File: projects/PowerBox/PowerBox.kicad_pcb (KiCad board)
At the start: 2 copper layers, 91.4 x 56.9 mm, 119 parts, among them CON1 USB-MICRO, CON2 USB-A-Jack, CON3 USB-MINI-B-Vert, IC1 LM358, IC2 LM358, IC3 LM358, P1 CONN_2, P11 CONN_10, P12 CONN_8, P13 CONN_8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

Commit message: pcb layout still in progress
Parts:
- moved D14 45.5 mm to (178.3, 110.5), turned to 180 degrees
- moved R32 45.5 mm to (178.3, 110.5), turned to 180 degrees
- moved D13 45.3 mm to (178.3, 106.7), turned to 180 degrees
- moved R31 45.3 mm to (178.3, 106.7), turned to 180 degrees
- moved JP2 23.6 mm to (155.2, 114.6)
- moved R20 18.4 mm to (117.9, 88.6)
- moved R16 16.9 mm to (119.4, 84.1), turned to 270 degrees
- moved R17 15.8 mm to (132.8, 81.0)
- moved R19 15.8 mm to (120.4, 93.2)
- moved R21 14.2 mm to (122.9, 83.1)
- moved R23 13.9 mm to (122.9, 88.6)
- moved R18 10.7 mm to (125.5, 93.2)
- moved R25 8.64 mm to (141.7, 114.6)
- moved R22 8.44 mm to (128.0, 88.6)
- moved R28 7.77 mm to (145.8, 106.7)
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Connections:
- net D7 renamed Clock
- U1 pad 10: V_MP -> VREG_in
- U3 pad 10: V_MP -> VREG_in
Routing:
- net VREG_in: track 111.4 -> 283.0 mm, vias 6 -> 9
- net Net-(JP1-Pad2): track 0.00 -> 56.1 mm, vias 0 -> 2
- net DIG1: track 0.00 -> 41.9 mm, vias 0 -> 1
- net SEGA: track 0.00 -> 41.8 mm
- net Net-(C4-Pad1): track 27.2 -> 63.3 mm, vias 0 -> 1
- net Net-(R7-Pad1): track 0.00 -> 35.9 mm
- net SEGE: track 0.00 -> 34.2 mm, vias 0 -> 2
- net SEGF: track 0.00 -> 32.7 mm, vias 0 -> 2
- net SEGB: track 0.00 -> 32.6 mm, vias 0 -> 2
- net SEGC: track 0.27 -> 31.8 mm, vias 0 -> 2
- net SEGD: track 0.00 -> 31.2 mm, vias 0 -> 2
- net TXLED: track 0.00 -> 30.1 mm, vias 0 -> 2
- net Net-(R8-Pad1): track 0.00 -> 27.9 mm
- net SEGDP: track 0.00 -> 24.4 mm
- net DIG2: track 0.00 -> 23.5 mm
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
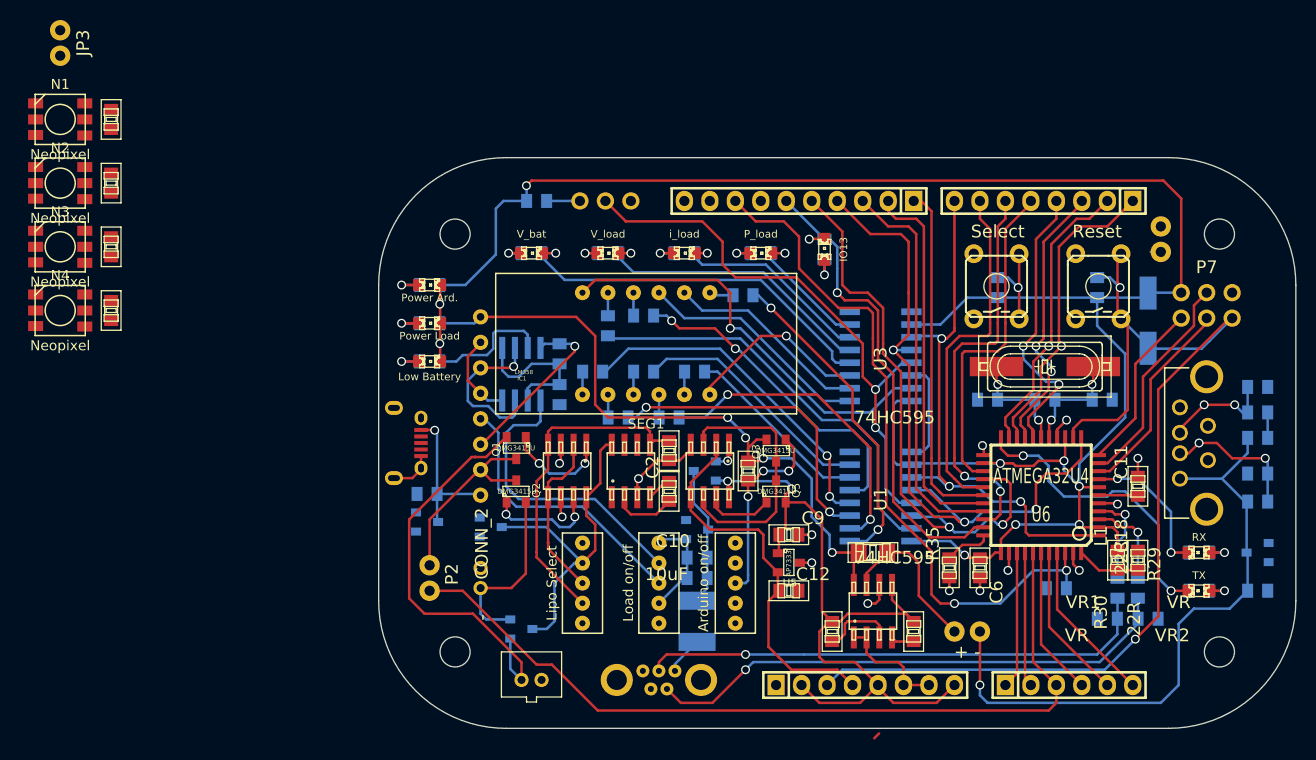
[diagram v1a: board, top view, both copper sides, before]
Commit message: pcb layout most traces done
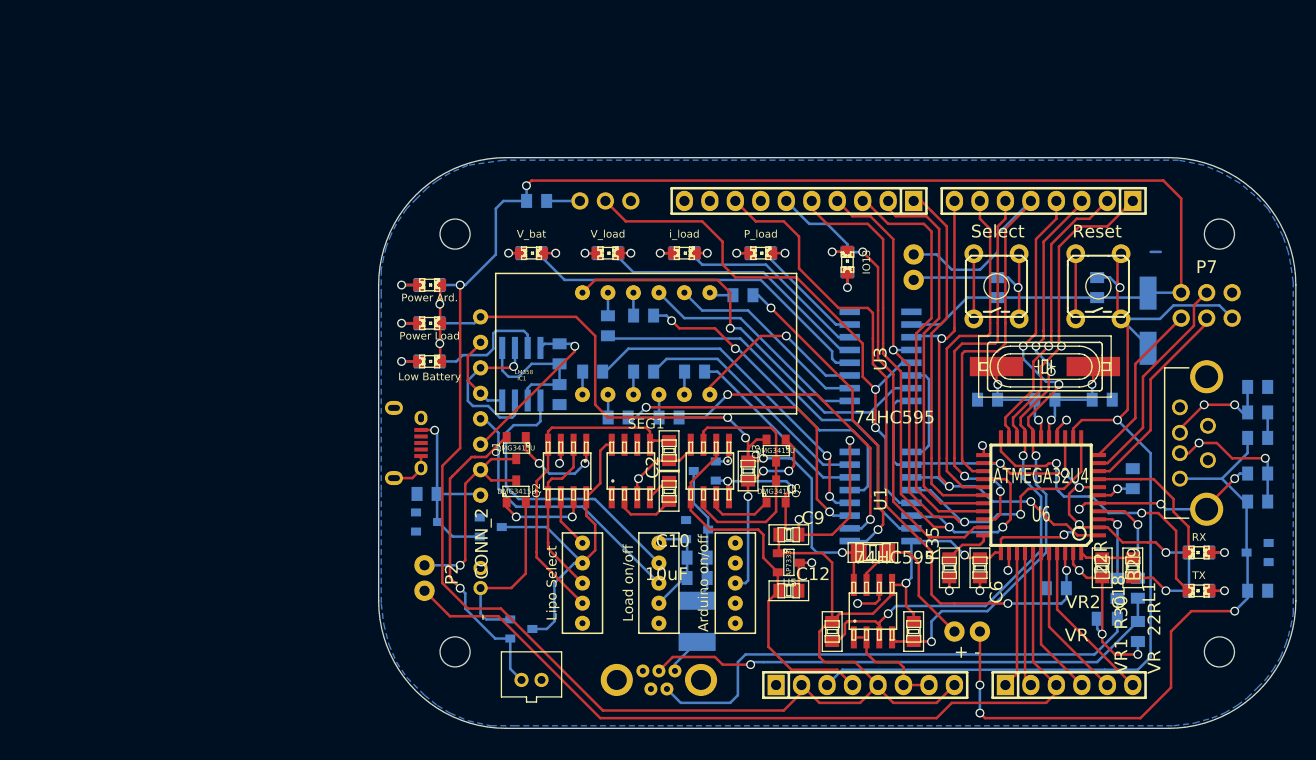
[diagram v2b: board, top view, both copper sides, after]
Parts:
- removed C13, C14, C15, C17: 100nF, frep:C0805
- removed JP3: JUMPER, frep:Pin_Proto_Straight_1x02
- removed N1, N2, N3, N4: Neopixel, frep:Neopixel
- C11: moved to B.Cu
- moved JP5 24.8 mm to (149.9, 78.2)
- moved VR2 4.06 mm to (169.2, 113.3), turned to 180 degrees
- moved C18 3.64 mm to (168.7, 108.2), turned to 270 degrees
- moved VR1 3.30 mm to (172.2, 114.6), turned to 270 degrees
- moved D16 2.62 mm to (143.3, 77.7)
- moved R34 2.62 mm to (143.3, 77.7)
- moved R29 2.03 mm to (170.2, 110.2)
- moved R30 2.03 mm to (172.2, 110.2)
- moved L1 1.70 mm to (171.7, 108.2), turned to 270 degrees
- moved C11 0.92 mm to (171.7, 99.3)
- moved JP4 0.51 mm to (101.1, 109.2)
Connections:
- net Clock renamed D7
- net IO_12 renamed Data
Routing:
- net VREG_in: track 283.0 -> 352.5 mm, vias 9 -> 13
- net GND: track 80.7 -> 147.2 mm, vias 21 -> 24
- net D2/SDA: track 35.4 -> 68.0 mm, vias 2 -> 4
- net D3/SCL: track 30.8 -> 60.9 mm, vias 2 -> 4
- net D4: track 33.3 -> 49.5 mm
- net Net-(D4-Pad1): track 41.3 -> 31.4 mm, vias 0 -> 1
- net Net-(JP5-Pad2): track 10.0 -> 17.8 mm
- net RESET: track 109.3 -> 101.7 mm
- net Net-(C1-Pad1): track 15.2 -> 19.9 mm
- net Net-(C4-Pad1): track 63.3 -> 65.8 mm, vias 1 -> 3
- net IO_10: track 39.8 -> 42.1 mm
- net V_BATT: track 19.7 -> 22.0 mm, vias 0 -> 1
- net Net-(IC2-Pad7): track 11.3 -> 9.43 mm
- net IO_9: track 37.8 -> 39.6 mm
- net Latch: track 68.1 -> 66.4 mm
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- added copper zone on B.Cu, net GND

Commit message: traces done
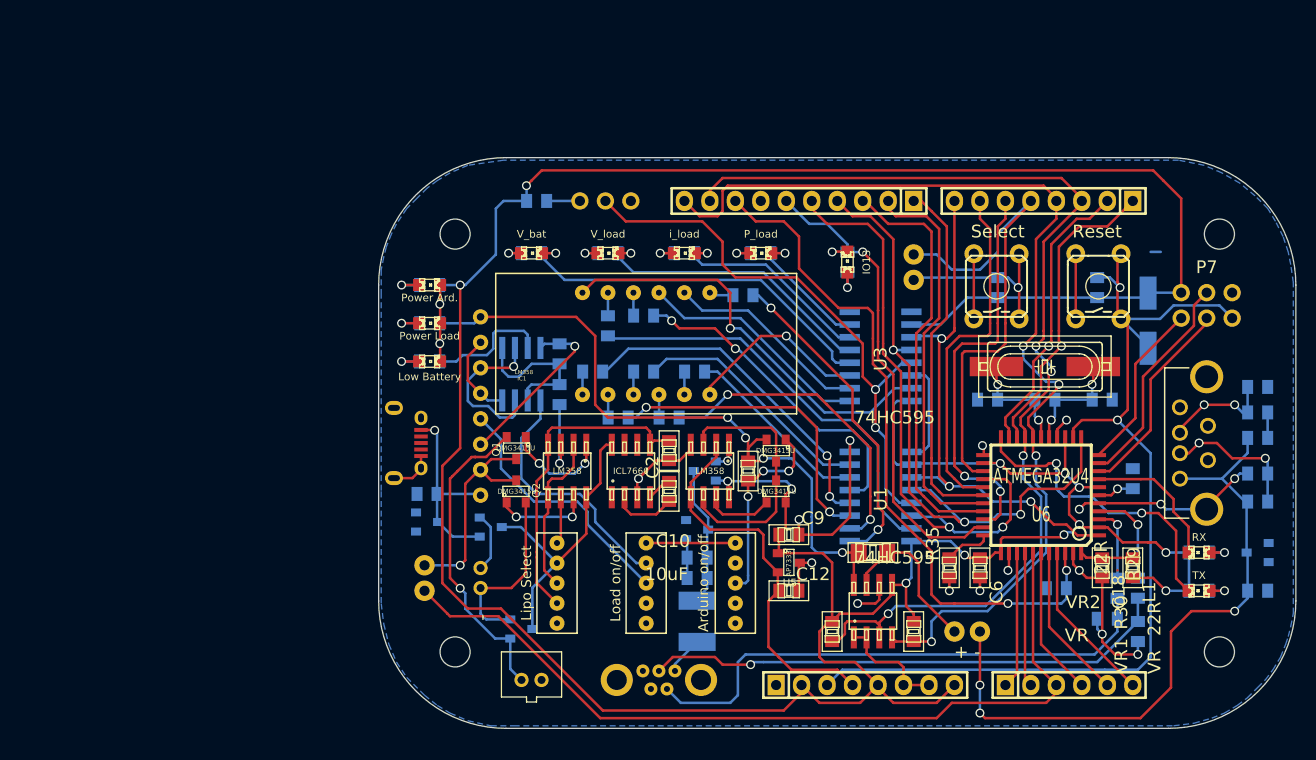
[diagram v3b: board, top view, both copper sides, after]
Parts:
- moved S1 2.54 mm to (114.3, 109.7)
- moved S2 1.27 mm to (123.2, 109.7)
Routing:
- net D3/SCL: track 60.9 -> 101.9 mm
- net D2/SDA: track 68.0 -> 107.7 mm
- net GND: track 147.2 -> 160.8 mm
- net V+: track 33.5 -> 29.0 mm
- net En: track 29.7 -> 25.3 mm
- net Enable: track 28.5 -> 26.3 mm
- net V-: track 34.3 -> 33.3 mm
- net LipoSwitch: track 18.0 -> 17.1 mm
- net VREG_in: track 352.5 -> 353.4 mm

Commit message: pcb still not finished
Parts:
- P7: value CONN_3X2 -> ICSP
- moved P2 5.84 mm to (100.8, 109.2)
- moved JP4 5.59 mm to (106.7, 109.2)
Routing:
- net Net-(C4-Pad1): track 65.8 -> 52.5 mm, vias 3 -> 2
- net A2: track 84.2 -> 77.6 mm
- net Net-(D4-Pad3): track 18.0 -> 22.4 mm, vias 0 -> 1
- net GND: track 160.8 -> 164.6 mm
- net VREG_in: track 353.4 -> 349.8 mm, vias 13 -> 15
- net V_BATT: track 22.0 -> 18.6 mm, vias 1 -> 0
- net A5: track 16.3 -> 18.6 mm
- net Net-(D4-Pad1): track 31.4 -> 29.7 mm
- net A4: track 15.6 -> 17.1 mm
- net A3: track 14.9 -> 15.6 mm

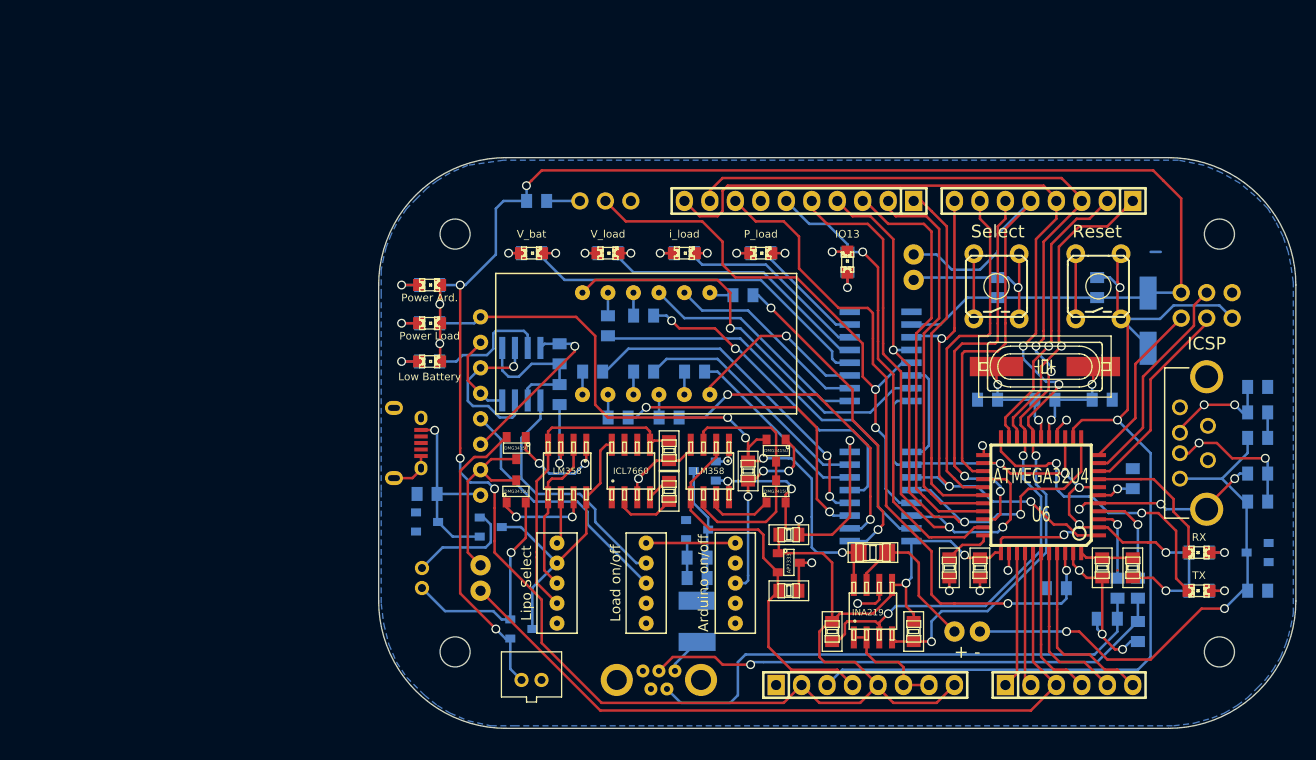
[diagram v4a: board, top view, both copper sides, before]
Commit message: start changing power lines
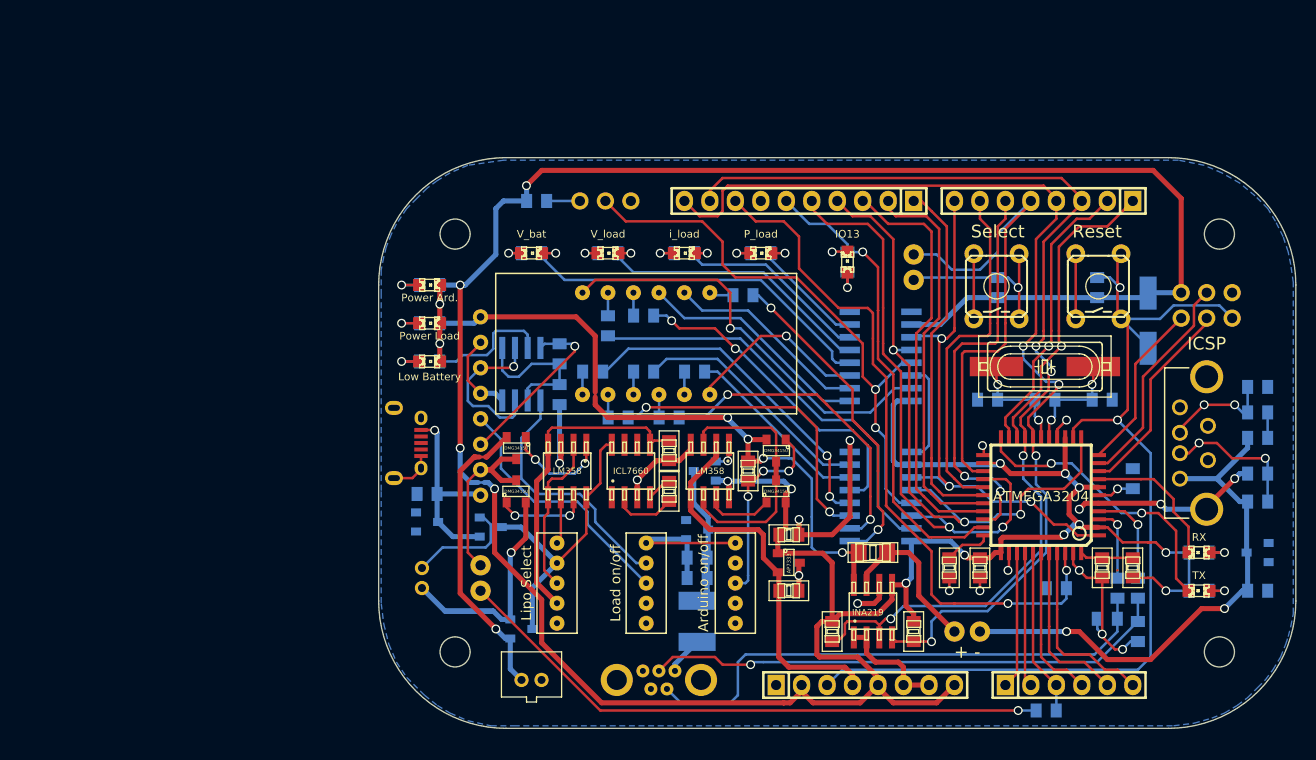
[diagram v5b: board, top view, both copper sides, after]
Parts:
- added R37: 10K, frep:R0805, B.Cu at (163.1, 122.4)
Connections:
- net Latch renamed IO_11
- JP4 pad 1: A2 -> Net-(JP4-Pad1)
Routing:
- net A2: track 77.6 -> 16.7 mm
- net Net-(JP4-Pad1): track 0.00 -> 60.3 mm, vias 0 -> 1
- net /Arduino/Vin+: track 67.6 -> 90.0 mm
- net GND: track 164.6 -> 184.5 mm
- net VREG_in: track 349.8 -> 365.4 mm
- net Net-(D4-Pad3): track 22.4 -> 27.3 mm
- net /Arduino/Vin-: track 16.0 -> 18.9 mm
- net TXLED: track 30.3 -> 28.8 mm
- net D2/SDA: track 107.7 -> 106.3 mm
- net Net-(C4-Pad1): track 52.5 -> 53.8 mm
- net 3V3: track 38.0 -> 39.3 mm
- net (no net): track 1.04 -> 0.03 mm
- net Net-(D4-Pad1): track 29.7 -> 30.4 mm
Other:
- net class Power added: clearance 0.254, trace_width 0.508, via_dia 0.889, via_drill 0.635

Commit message: arduino pins labled
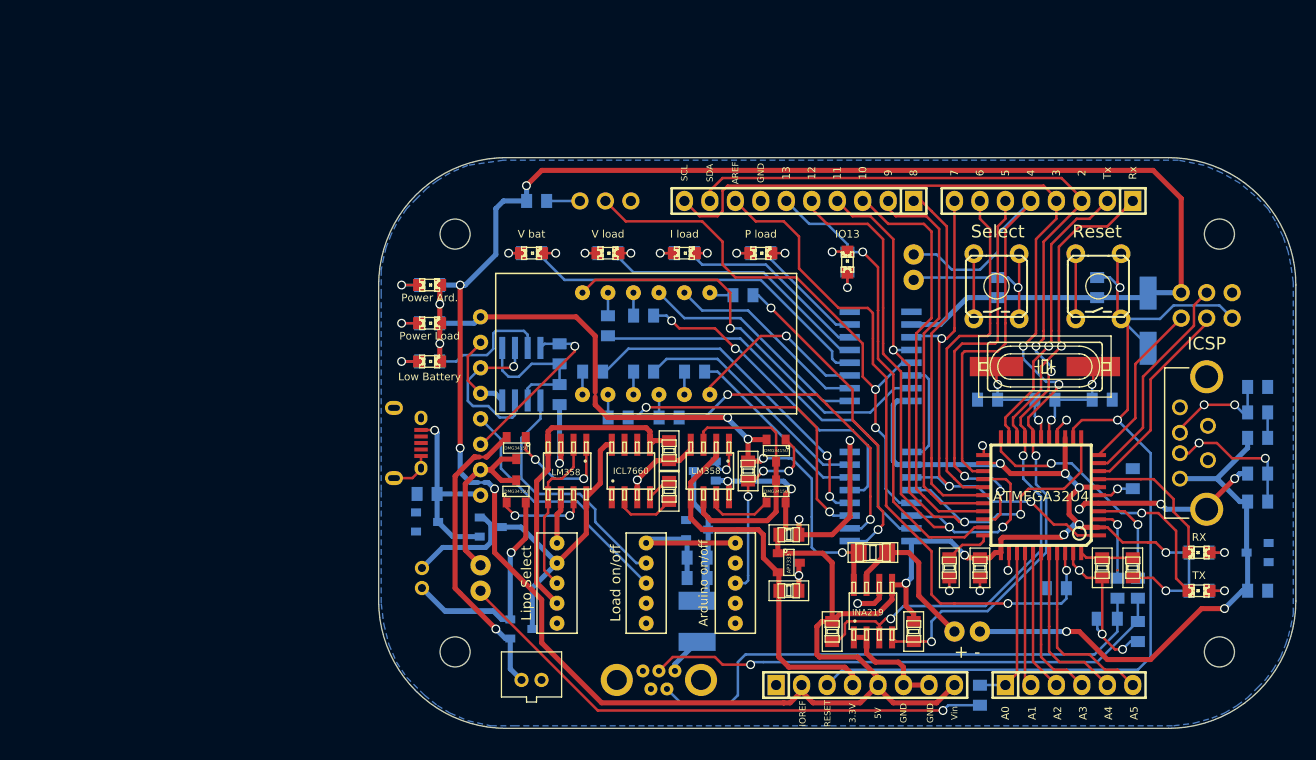
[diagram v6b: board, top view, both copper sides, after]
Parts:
- D6: value V_bat -> V bat
- D7: value V_load -> V load
- D8: value i_load -> I load
- D9: value P_load -> P load
- moved R37 6.78 mm to (156.5, 120.9), turned to 270 degrees
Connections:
- net Data renamed IO_12
- R37 pad 1: A2 -> A0
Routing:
- net Net-(JP4-Pad1): track 60.3 -> 55.1 mm
- net A2: track 16.7 -> 14.2 mm
- net A0: track 13.7 -> 16.2 mm
- net Net-(IC3-Pad1): track 2.87 -> 4.16 mm
- net /Arduino/VCC: track 26.1 -> 27.4 mm
- net Net-(IC2-Pad1): track 10.9 -> 12.1 mm
- net 3V3: track 39.3 -> 38.4 mm
- net V-: track 33.3 -> 33.9 mm
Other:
- board text added: "10"
- board text added: "11"
- board text added: "12"
- board text added: "13"
- board text added: "2"
- board text added: "3"
- board text added: "3.3V"
- board text added: "4"
- board text added: "5"
- board text added: "5V"
- board text added: "6"
- board text added: "7"
- board text added: "8"
- board text added: "9"
- board text added: "A0"
- board text added: "A1"
- board text added: "A2"
- board text added: "A3"
- board text added: "A4"
- board text added: "A5"
- board text added: "AREF"
- board text added: "GND"
- board text added: "IOREF"
- board text added: "RESET"
- board text added: "Rx"
- board text added: "SCL"
- board text added: "SDA"
- board text added: "Tx"
- board text added: "Vin"
